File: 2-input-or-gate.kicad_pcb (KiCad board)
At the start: 2 copper layers, 9.4 x 11.1 mm, 11 parts, among them U5 74LVC1G332GW,125

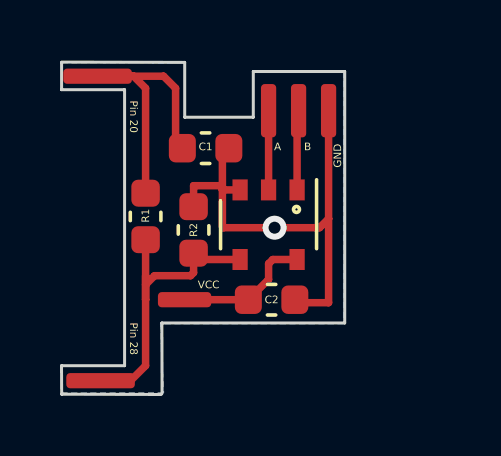
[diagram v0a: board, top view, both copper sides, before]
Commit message: updated design to be larger with larger pads. Got rid of 1k resistor.
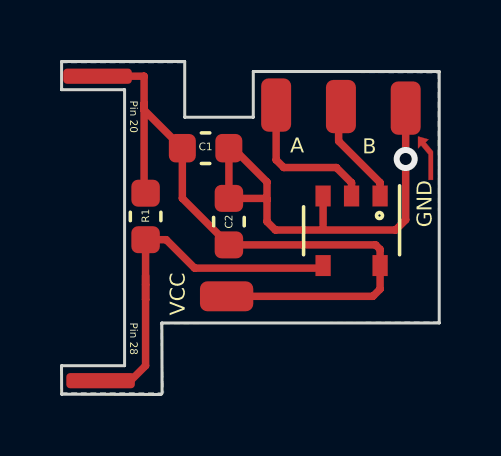
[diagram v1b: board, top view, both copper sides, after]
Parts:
- removed R2: 0.01uf, Capacitor_SMD:C_0603_1608Metric
- moved C2 2.97 mm to (147.8, 96.7), turned to 90 degrees
- moved U5 2.77 mm to (151.9, 97.0)
- moved ? 2.57 mm to (153.7, 92.9)
- moved ? 1.42 mm to (151.5, 92.9)
- moved ? 1.41 mm to (147.7, 99.2), turned to 180 degrees
- moved ? 0.31 mm to (149.4, 92.8)
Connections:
- ? pad 1: VCC-PAD -> VCC5V
- C1 pad 5: VCC-PAD -> VCC5V
- R1 pad 2: VCC-PAD -> VCC5V
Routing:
- net VCC5V: track 4.61 -> 23.6 mm
- net VCC-PAD: track 10.2 -> 0.00 mm
- net A: track 2.64 -> 5.10 mm
- net CE: track 10.8 -> 13.1 mm
- net B: track 2.66 -> 3.55 mm
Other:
- board size 9.4 x 11.1 mm -> 12.6 x 11.1 mm
